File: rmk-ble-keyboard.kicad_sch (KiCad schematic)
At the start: 0 parts

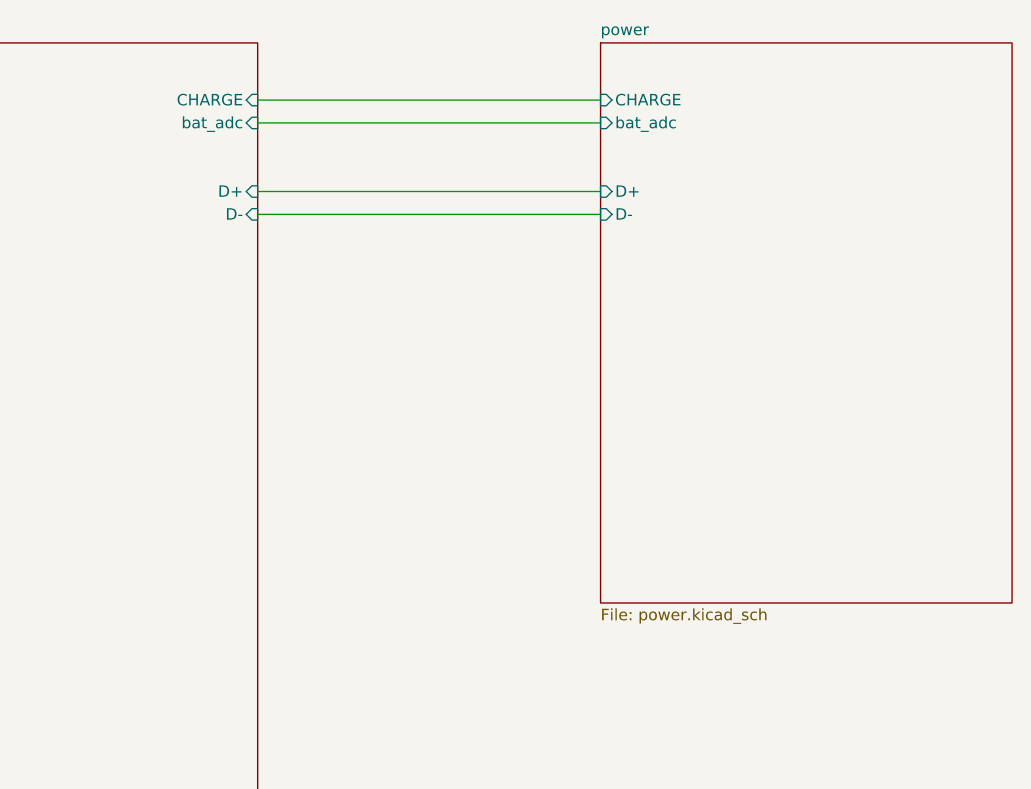
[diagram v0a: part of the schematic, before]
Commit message: update rmk-ble-keyboard %65
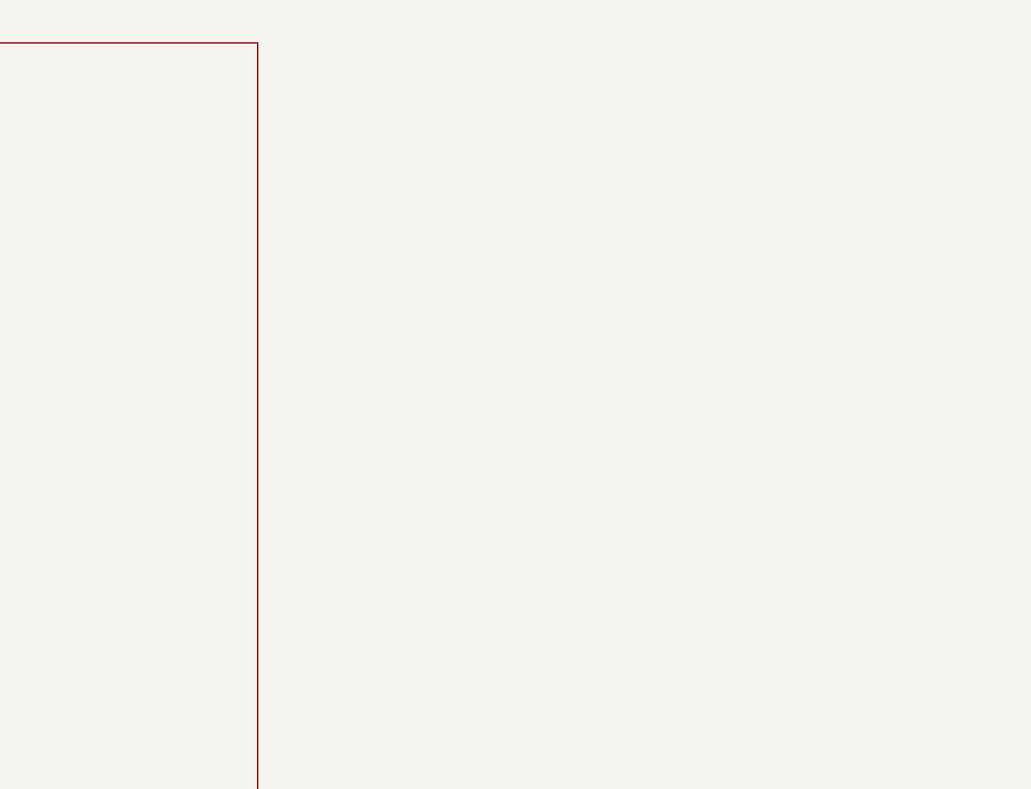
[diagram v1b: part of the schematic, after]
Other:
- removed sheet power
- sheet mcu ports: added none; removed CHARGE, D+, D-, bat_adc
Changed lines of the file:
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@@
-	(wire
-		(pts
-			(xy 165.1 44.45) (xy 203.2 44.45)
-		)
-		(stroke
-			(width 0)
-			(type default)
-		)
-	)
 	(wire
 		(pts
@@
 	(wire
 		(pts
-			(xy 165.1 34.29) (xy 203.2 34.29)
-		)
-		(stroke
-			(width 0)
-			(type default)
-		)
-	)
-	(wire
-		(pts
 			(xy 76.2 48.26) (xy 101.6 48.26)
 		)
@@
 	(wire
 		(pts
-			(xy 165.1 41.91) (xy 203.2 41.91)
-		)
-		(stroke
-			(width 0)
-			(type default)
-		)
-	)
-	(wire
-		(pts
 			(xy 76.2 86.36) (xy 101.6 86.36)
 		)
@@
 		(pts
 			(xy 76.2 33.02) (xy 101.6 33.02)
-		)
-		(stroke
-			(width 0)
-			(type default)
-		)
-	)
-	(wire
-		(pts
-			(xy 165.1 31.75) (xy 203.2 31.75)
 		)
 		(stroke
@@
 			)
 		)
-		(pin "CHARGE" input
-			(at 165.1 31.75 0)
-			(effects
-				(font
-					(size 1.27 1.27)
-				)
-				(justify right)
-			)
-		)
 		(pin "col10" input
 			(at 101.6 55.88 180)
@@
 			)
 		)
-		(pin "D+" input
-			(at 165.1 41.91 0)
-			(effects
-				(font
-					(size 1.27 1.27)
-				)
-				(justify right)
-			)
-		)
 		(pin "col12" input
 			(at 101.6 60.96 180)
@@
 				)
 				(justify left)
-			)
-		)
-		(pin "D-" input
-			(at 165.1 44.45 0)
-			(effects
-				(font
-					(size 1.27 1.27)
-				)
-				(justify right)
-			)
-		)
-		(pin "bat_adc" input
-			(at 165.1 34.29 0)
-			(effects
-				(font
-					(size 1.27 1.27)
-				)
-				(justify right)
 			)
 		)
@@
 				)
 			)
-		)
-	)
-	(sheet
-		(at 203.2 25.4)
-		(size 45.72 62.23)
-		(fields_autoplaced yes)
-		(stroke
-			(width 0.1524)
-			(type solid)
-		)
-		(fill
-			(color 0 0 0 0.0000)
-		)
-		(property "Sheetname" "power"
-			(at 203.2 24.6884 0)
-			(effects
-				(font
-					(size 1.27 1.27)
-				)
-				(justify left bottom)
-			)
-		)
-		(property "Sheetfile" "power.kicad_sch"
-			(at 203.2 88.2146 0)
-			(effects
-				(font
-					(size 1.27 1.27)
-				)
-				(justify left top)
-			)
-		)
-		(pin "D+" input
-			(at 203.2 41.91 180)
-			(effects
-				(font
-					(size 1.27 1.27)
-				)
-				(justify left)
-			)
-		)
-		(pin "D-" input
-			(at 203.2 44.45 180)
-			(effects
-				(font
-					(size 1.27 1.27)
-				)
-				(justify left)
-			)
-		)
-		(pin "CHARGE" input
-			(at 203.2 31.75 180)
-			(effects
-				(font
-					(size 1.27 1.27)
-				)
-				(justify left)
-			)
-		)
-		(pin "bat_adc" input
-			(at 203.2 34.29 180)
-			(effects
-				(font
-					(size 1.27 1.27)
-				)
-				(justify left)
-			)
-		)
-		(instances
-			(project "rmk-ble-keyboard"
-				(path "/5823a915-d0ed-4262-9b2d-d2247405cf69"
-					(page "3")
-				)
-			)
